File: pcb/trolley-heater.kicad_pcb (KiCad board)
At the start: 2 copper layers, 160 x 65 mm, 48 parts, among them K1 RELAY_SPDT, K2 RELAY_SPDT, K3 RELAY_SPDT, K4 RELAY_SPDT, K5 RELAY_SPDT, K6 RELAY_SPDT, P1 CONN_01X03, P10 CONN_01X02, P2 CONN_01X03, P3 CONN_01X03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

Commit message: updated: prepare for 1.0 release.
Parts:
- moved P10 23.0 mm to (213.0, 41.0), turned to 0 degrees
- moved P8 19.0 mm to (185.0, 41.0), turned to 0 degrees
- moved P9 19.0 mm to (199.0, 41.0), turned to 0 degrees
- moved P5 5.00 mm to (143.0, 41.0), turned to 0 degrees
- moved P6 5.00 mm to (157.0, 41.0), turned to 0 degrees
- moved P7 5.00 mm to (171.0, 41.0), turned to 0 degrees
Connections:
- P10 pad 1: Net-(K4-Pad14) -> Net-(K6-Pad11)
- P10 pad 2: Net-(K4-Pad11) -> Net-(K6-Pad14)
- P5 pad 1: Net-(K1-Pad14) -> Net-(K1-Pad11)
- P5 pad 2: Net-(K1-Pad11) -> Net-(K1-Pad14)
- P6 pad 1: Net-(K2-Pad14) -> Net-(K2-Pad11)
- P6 pad 2: Net-(K2-Pad11) -> Net-(K2-Pad14)
- P7 pad 1: Net-(K3-Pad14) -> Net-(K3-Pad11)
- P7 pad 2: Net-(K3-Pad11) -> Net-(K3-Pad14)
- P8 pad 1: Net-(K5-Pad14) -> Net-(K4-Pad11)
- P8 pad 2: Net-(K5-Pad11) -> Net-(K4-Pad14)
- P9 pad 1: Net-(K6-Pad14) -> Net-(K5-Pad11)
- P9 pad 2: Net-(K6-Pad11) -> Net-(K5-Pad14)
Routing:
- net GNDREF: track 182.4 -> 260.0 mm, vias 0 -> 1
- net /D/C: track 0.00 -> 73.9 mm, vias 0 -> 1
- net +5V: track 198.8 -> 261.6 mm
- net +3V3: track 0.00 -> 53.5 mm, vias 0 -> 2
- net /CH1_IN: track 0.00 -> 40.8 mm
- net /CH3_IN: track 0.00 -> 35.6 mm
- net /CH2_IN: track 0.00 -> 34.8 mm
- net /RST: track 0.00 -> 29.3 mm, vias 0 -> 1
- net /MISO: track 0.00 -> 27.2 mm
- net /MOSI: track 0.00 -> 17.7 mm
- net /SCLK: track 0.00 -> 16.3 mm
- net /CS: track 0.00 -> 12.8 mm
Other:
- board text added: "Designed by Isaac 2017"
- board text removed: "By Isaac Channells - 2016"

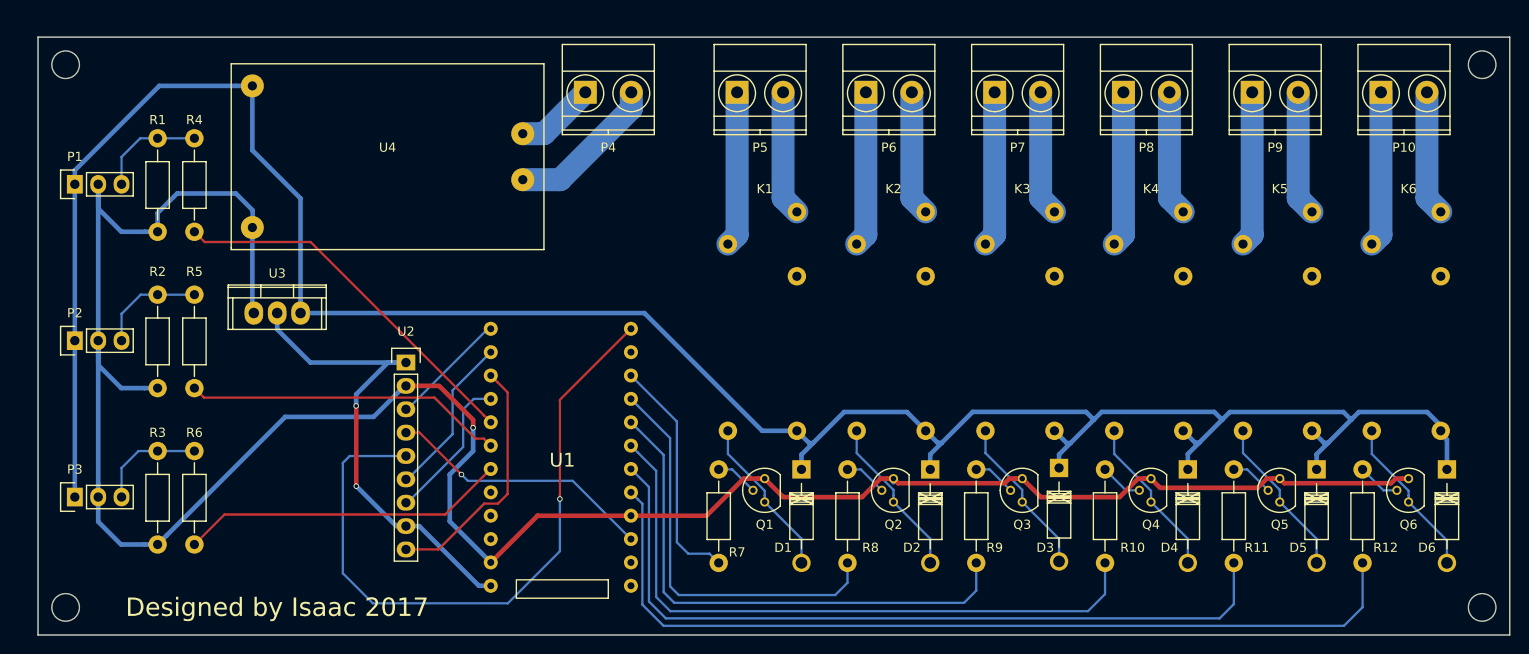
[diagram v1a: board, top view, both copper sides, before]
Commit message: updated: with fill and additional mains filtering.
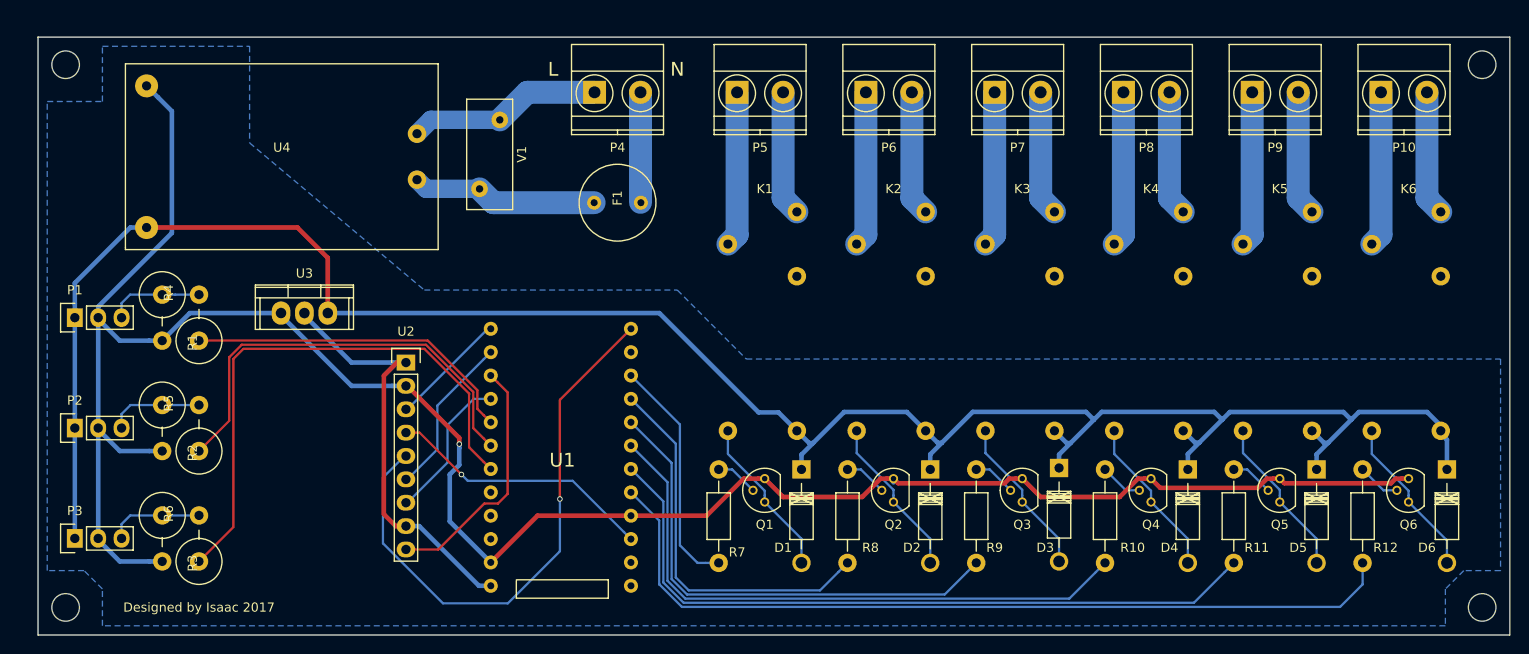
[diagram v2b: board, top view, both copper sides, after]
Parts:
- added F1: 0.8A, components:Fuse_Radial, F.Cu at (130.0, 53.0)
- added V1: 275V, Varistors:RV_Disc_D12_W5_P7.5, F.Cu at (115.0, 51.5)
- R1, R2, R3, R4, R5, R6: footprint Resistors_ThroughHole:Resistor_Horizontal_RM10mm -> Resistors_ThroughHole:Resistor_Vertical_RM5mm
- moved R1 19.5 mm to (80.5, 65.5)
- moved R2 14.5 mm to (80.5, 77.5)
- moved P1 14.5 mm to (71.0, 65.5)
- moved U4 11.5 mm to (93.5, 48.0)
- moved R3 9.51 mm to (80.5, 89.5)
- moved P2 9.50 mm to (71.0, 77.5)
- moved R4 9.35 mm to (84.5, 65.5)
- moved P3 4.50 mm to (71.0, 89.5)
- moved R5 4.37 mm to (84.5, 77.5)
- moved U3 2.96 mm to (96.0, 65.0)
- moved P4 1.00 mm to (127.5, 41.0)
- moved R6 0.83 mm to (84.5, 89.5)
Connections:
- P4 pad 2: Net-(P4-Pad2) -> Net-(F1-Pad1)
- U4 pad 1: Net-(P4-Pad2) -> Net-(F1-Pad2)
- U4 pad 3: GNDREF -> +5V
- U4 pad 4: +5V -> GNDREF
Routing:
- net /CH3_IN: track 35.6 -> 60.8 mm
- net +5V: track 261.6 -> 238.3 mm
- net Net-(F1-Pad2): track 0.00 -> 20.3 mm
- net GNDREF: track 260.0 -> 242.1 mm
- net Net-(P4-Pad2): track 17.6 -> 0.00 mm
- net /CH2_IN: track 34.8 -> 47.4 mm
- net Net-(F1-Pad1): track 0.00 -> 12.0 mm
- net /D/C: track 73.9 -> 62.3 mm
- net Net-(P4-Pad1): track 10.00 -> 21.2 mm
- net +3V3: track 53.5 -> 46.3 mm, vias 2 -> 0
- net /CH4_OUT: track 84.7 -> 78.5 mm
- net /CH6_OUT: track 97.6 -> 92.1 mm
- net /CH2_OUT: track 71.2 -> 66.3 mm
- net /CH1_IN: track 40.8 -> 36.6 mm
- net /CH5_OUT: track 58.0 -> 54.1 mm
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- added copper zone on B.Cu, net GNDREF
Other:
- board text added: "L"
- board text added: "N"

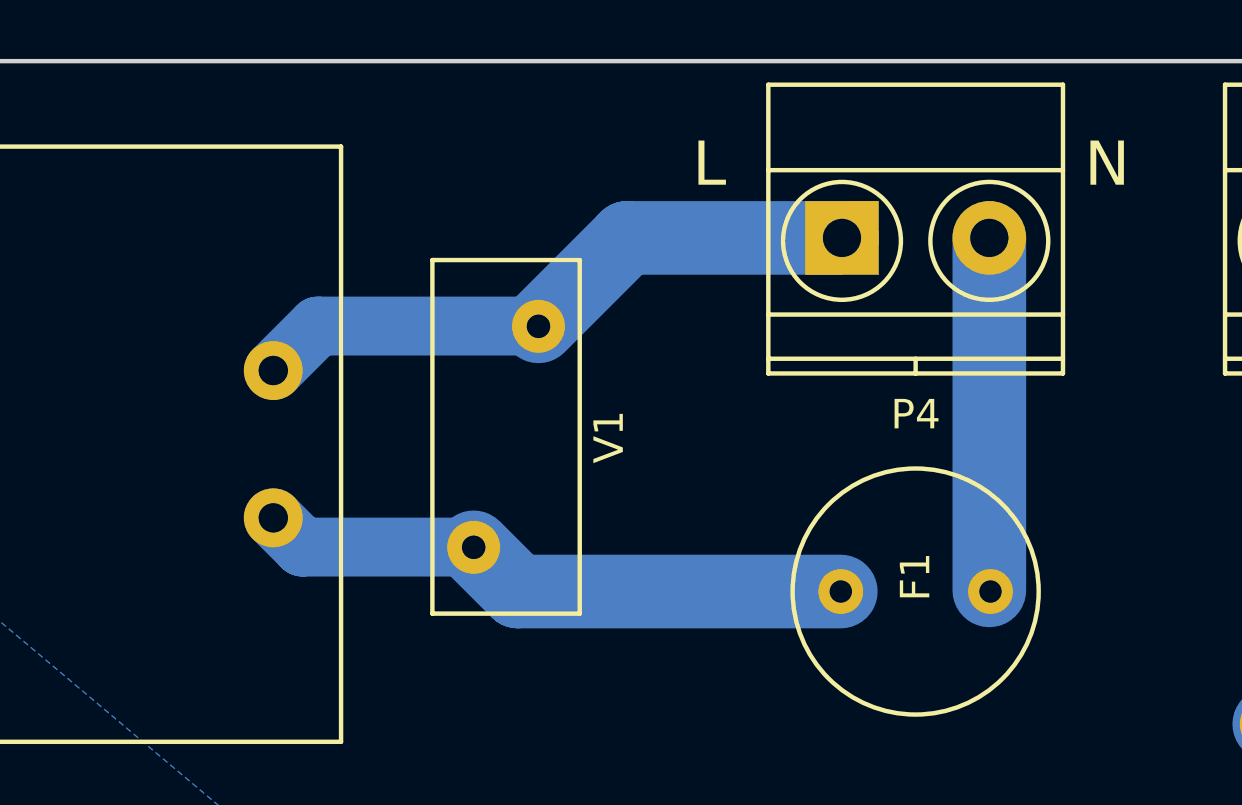
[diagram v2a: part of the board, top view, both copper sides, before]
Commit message: updated: tweaking ac input connector and battery pack support.
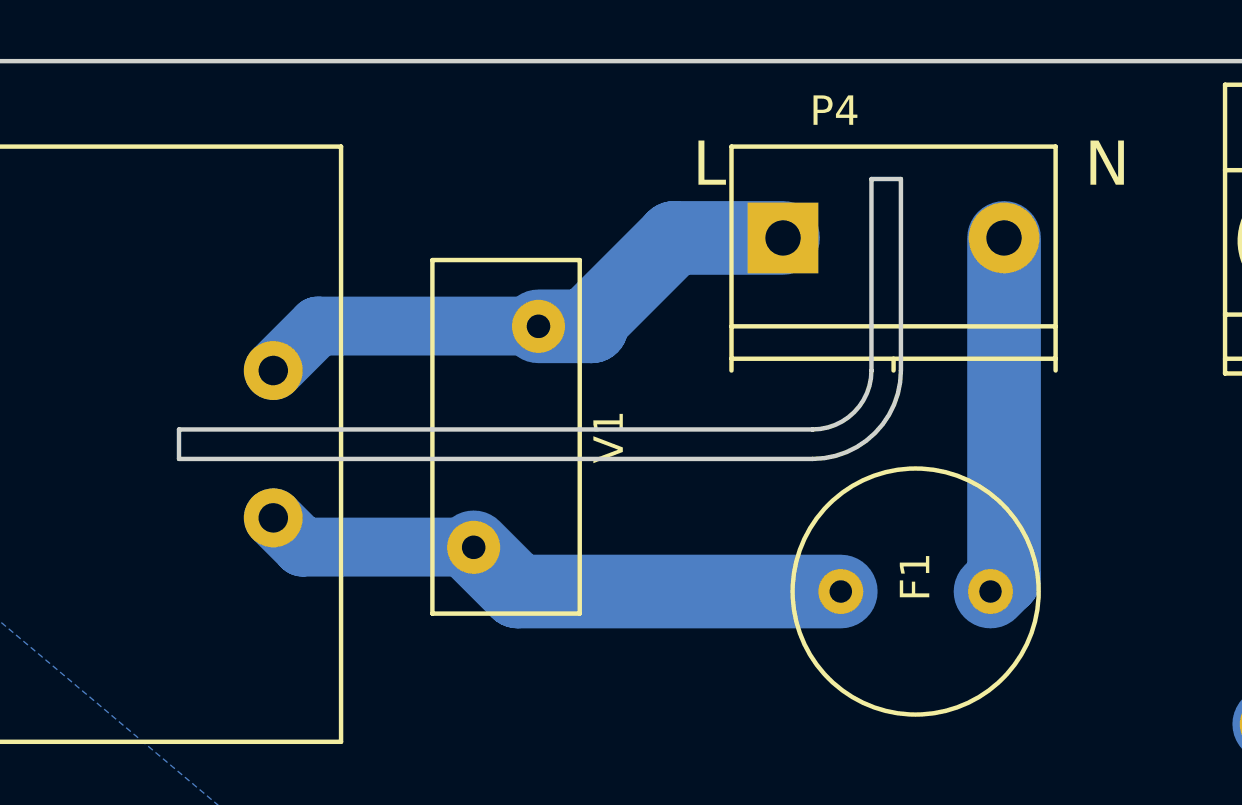
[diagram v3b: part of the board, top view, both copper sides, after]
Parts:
- P4: footprint Terminal_Blocks:TerminalBlock_Pheonix_MKDS1.5-2pol -> components:TerminalBlock_Pheonix_PT-7.5mm_2pol
- moved P4 2.00 mm to (125.5, 41.0)
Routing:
- net Net-(P4-Pad1): track 21.2 -> 19.3 mm
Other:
- outline, holes or cut-outs redrawn
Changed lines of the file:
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@@
   (general
     (links 91)
-    (no_connects 0)
+    (no_connects 2)
     (area 66.924999 34.924999 227.075001 100.075001)
     (thickness 1.6)
-    (drawings 7)
-    (tracks 329)
+    (drawings 15)
+    (tracks 332)
     (zones 0)
     (modules 50)
@@
       (net 2 +5V))
   )
-  (module Terminal_Blocks:TerminalBlock_Pheonix_MKDS1.5-2pol (layer F.Cu)
-    (at 127.5 41)
-    (descr "2-way 5mm pitch terminal block, Phoenix MKDS series")
-    (fp_text reference P4 (at 2.5 6 180) (layer F.SilkS)
-      (effects (font (size 1 1) (thickness 0.15)))
-    )
-    (fp_text value CONN_01X02 (at 2.5 -6.6) (layer F.Fab)
-      (effects (font (size 1 1) (thickness 0.15)))
-    )
-    (fp_line (start -2.7 -5.4) (end 7.7 -5.4) (layer F.CrtYd) (width 0.05))
-    (fp_line (start -2.7 4.8) (end -2.7 -5.4) (layer F.CrtYd) (width 0.05))
-    (fp_line (start 7.7 4.8) (end -2.7 4.8) (layer F.CrtYd) (width 0.05))
-    (fp_line (start 7.7 -5.4) (end 7.7 4.8) (layer F.CrtYd) (width 0.05))
-    (fp_line (start 2.5 4.1) (end 2.5 4.6) (layer F.SilkS) (width 0.15))
-    (fp_circle (center 5 0.1) (end 3 0.1) (layer F.SilkS) (width 0.15))
-    (fp_circle (center 0 0.1) (end 2 0.1) (layer F.SilkS) (width 0.15))
-    (fp_line (start -2.5 2.6) (end 7.5 2.6) (layer F.SilkS) (width 0.15))
-    (fp_line (start -2.5 -2.3) (end 7.5 -2.3) (layer F.SilkS) (width 0.15))
-    (fp_line (start -2.5 4.1) (end 7.5 4.1) (layer F.SilkS) (width 0.15))
-    (fp_line (start -2.5 4.6) (end 7.5 4.6) (layer F.SilkS) (width 0.15))
-    (fp_line (start 7.5 4.6) (end 7.5 -5.2) (layer F.SilkS) (width 0.15))
-    (fp_line (start 7.5 -5.2) (end -2.5 -5.2) (layer F.SilkS) (width 0.15))
-    (fp_line (start -2.5 -5.2) (end -2.5 4.6) (layer F.SilkS) (width 0.15))
-    (pad 1 thru_hole rect (at 0 0) (size 2.5 2.5) (drill 1.3) (layers *.Cu *.Mask F.SilkS)
-      (net 46 "Net-(P4-Pad1)"))
-    (pad 2 thru_hole circle (at 5 0) (size 2.5 2.5) (drill 1.3) (layers *.Cu *.Mask F.SilkS)
-      (net 47 "Net-(F1-Pad1)"))
-    (model Terminal_Blocks.3dshapes/TerminalBlock_Pheonix_MKDS1.5-2pol.wrl
-      (at (xyz 0.0984 0 0))
-      (scale (xyz 1 1 1))
-      (rotate (xyz 0 0 180))
-    )
-  )
   (module TO_SOT_Packages_THT:TO-92_Molded_Narrow (layer F.Cu)
     (at 146 85.54 90)
@@
       (net 11 "Net-(P3-Pad3)"))
   )
+  (module components:TerminalBlock_Pheonix_PT-7.5mm_2pol (layer F.Cu)
+    (at 125.5 41)
+    (descr "2-way 3.5mm pitch terminal block, Phoenix PT series")
+    (fp_text reference P4 (at 1.75 -4.3) (layer F.SilkS)
+      (effects (font (size 1 1) (thickness 0.15)))
+    )
+    (fp_text value CONN_01X02 (at 1.75 6) (layer F.Fab)
+      (effects (font (size 1 1) (thickness 0.15)))
+    )
+    (fp_line (start -1.9 -3.3) (end 9.4 -3.3) (layer F.CrtYd) (width 0.05))
+    (fp_line (start -1.9 4.7) (end -1.9 -3.3) (layer F.CrtYd) (width 0.05))
+    (fp_line (start 9.4 4.7) (end -1.9 4.7) (layer F.CrtYd) (width 0.05))
+    (fp_line (start 9.4 -3.3) (end 9.4 4.7) (layer F.CrtYd) (width 0.05))
+    (fp_line (start 3.75 4.1) (end 3.75 4.5) (layer F.SilkS) (width 0.15))
+    (fp_line (start -1.75 3) (end 9.25 3) (layer F.SilkS) (width 0.15))
+    (fp_line (start -1.75 4.1) (end 9.25 4.1) (layer F.SilkS) (width 0.15))
+    (fp_line (start -1.75 -3.1) (end -1.75 4.5) (layer F.SilkS) (width 0.15))
+    (fp_line (start 9.25 4.5) (end 9.25 -3.1) (layer F.SilkS) (width 0.15))
+    (fp_line (start 9.25 -3.1) (end -1.75 -3.1) (layer F.SilkS) (width 0.15))
+    (pad 2 thru_hole circle (at 7.5 0) (size 2.4 2.4) (drill 1.2) (layers *.Cu *.Mask F.SilkS)
+      (net 47 "Net-(F1-Pad1)"))
+    (pad 1 thru_hole rect (at 0 0) (size 2.4 2.4) (drill 1.2) (layers *.Cu *.Mask F.SilkS)
+      (net 46 "Net-(P4-Pad1)"))
+    (model Terminal_Blocks.3dshapes/TerminalBlock_Pheonix_PT-3.5mm_2pol.wrl
+      (at (xyz 0 0 0))
+      (scale (xyz 1 1 1))
+      (rotate (xyz 0 0 0))
+    )
+  )
+  (gr_arc (start 126.5 45.5) (end 129.5 45.5) (angle 90) (layer Edge.Cuts) (width 0.15))
+  (gr_arc (start 126.5 45.5) (end 128.5 45.5) (angle 90) (layer Edge.Cuts) (width 0.15))
+  (gr_line (start 105 48.5) (end 105 47.5) (layer Edge.Cuts) (width 0.15))
+  (gr_line (start 126.5 48.5) (end 105 48.5) (layer Edge.Cuts) (width 0.15))
+  (gr_line (start 129.5 39) (end 129.5 45.5) (layer Edge.Cuts) (width 0.15))
+  (gr_line (start 128.5 39) (end 129.5 39) (layer Edge.Cuts) (width 0.15))
+  (gr_line (start 128.5 45.5) (end 128.5 39) (layer Edge.Cuts) (width 0.15))
+  (gr_line (start 105 47.5) (end 126.5 47.5) (layer Edge.Cuts) (width 0.15))
   (gr_text N (at 136.5 38.5) (layer F.SilkS)
     (effects (font (size 1.5 1.5) (thickness 0.3)))
@@
   (segment (start 108.442139 88.16) (end 114.932139 94.65) (width 0.5) (layer B.Cu) (net 45))
   (segment (start 114.932139 94.65) (end 116.22 94.65) (width 0.5) (layer B.Cu) (net 45))
+  (segment (start 119 44) (end 119 43.8) (width 2.5) (layer B.Cu) (net 46))
+  (segment (start 119 43.8) (end 121.8 41) (width 2.5) (layer B.Cu) (net 46))
+  (segment (start 121.8 41) (end 125.5 41) (width 2.5) (layer B.Cu) (net 46))
+  (segment (start 117.2 44) (end 119 44) (width 2.5) (layer B.Cu) (net 46))
   (segment (start 108.2 45.5) (end 109.709665 43.990335) (width 2) (layer B.Cu) (net 46))
   (segment (start 109.709665 43.990335) (end 117.190335 43.990335) (width 2) (layer B.Cu) (net 46))
   (segment (start 117.190335 43.990335) (end 117.2 44) (width 2) (layer B.Cu) (net 46))
-  (segment (start 127.5 41) (end 120.2 41) (width 2.5) (layer B.Cu) (net 46))
-  (segment (start 120.2 41) (end 117.2 44) (width 2.5) (layer B.Cu) (net 46))
-  (segment (start 132.5 41) (end 132.5 52.96) (width 2.5) (layer B.Cu) (net 47))
+  (segment (start 133 41) (end 133 52.54) (width 2.5) (layer B.Cu) (net 47))
+  (segment (start 133 52.54) (end 132.54 53) (width 2.5) (layer B.Cu) (net 47))
   (segment (start 132.5 52.96) (end 132.54 53) (width 0.25) (layer B.Cu) (net 47))
   (segment (start 108.2 50.5) (end 109.191772 51.491772) (width 2) (layer B.Cu) (net 48))
